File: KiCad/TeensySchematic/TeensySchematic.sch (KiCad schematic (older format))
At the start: 4 parts, among them J1 LEFT_ESC, J2 RIGHT_ESC, U1 Teensy3.2, U2 BNO055

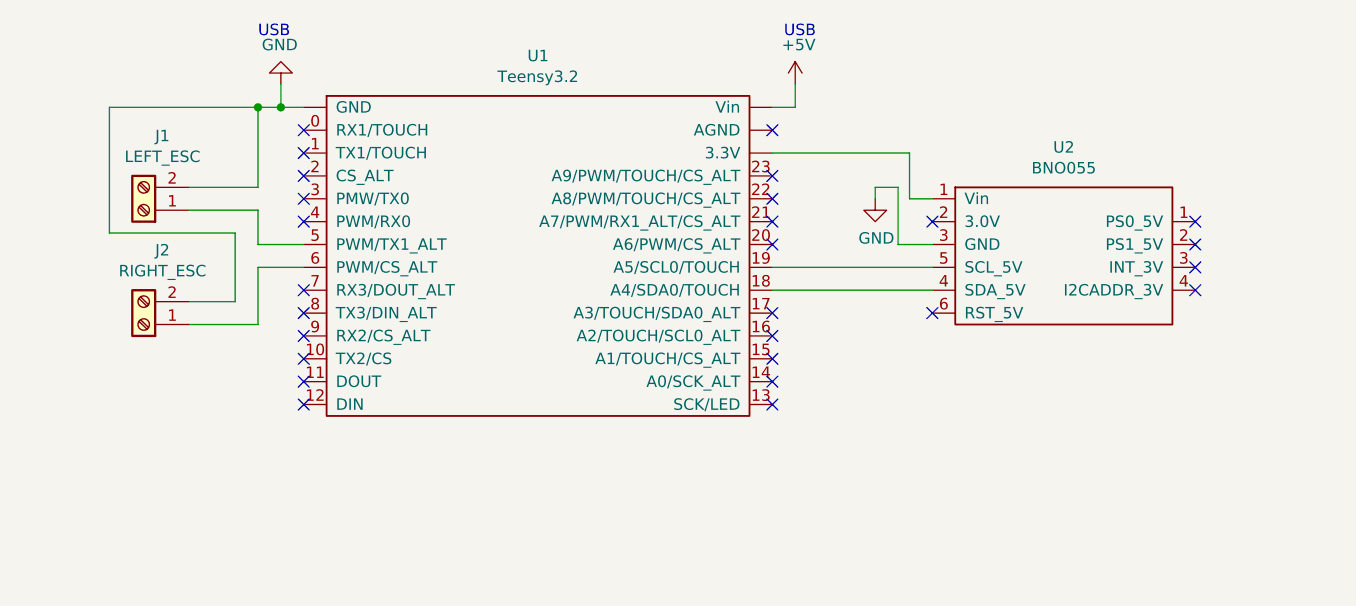
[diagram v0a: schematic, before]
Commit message: Added Ultimate GPS to the Teensy Schematic and updated our custom symbol library
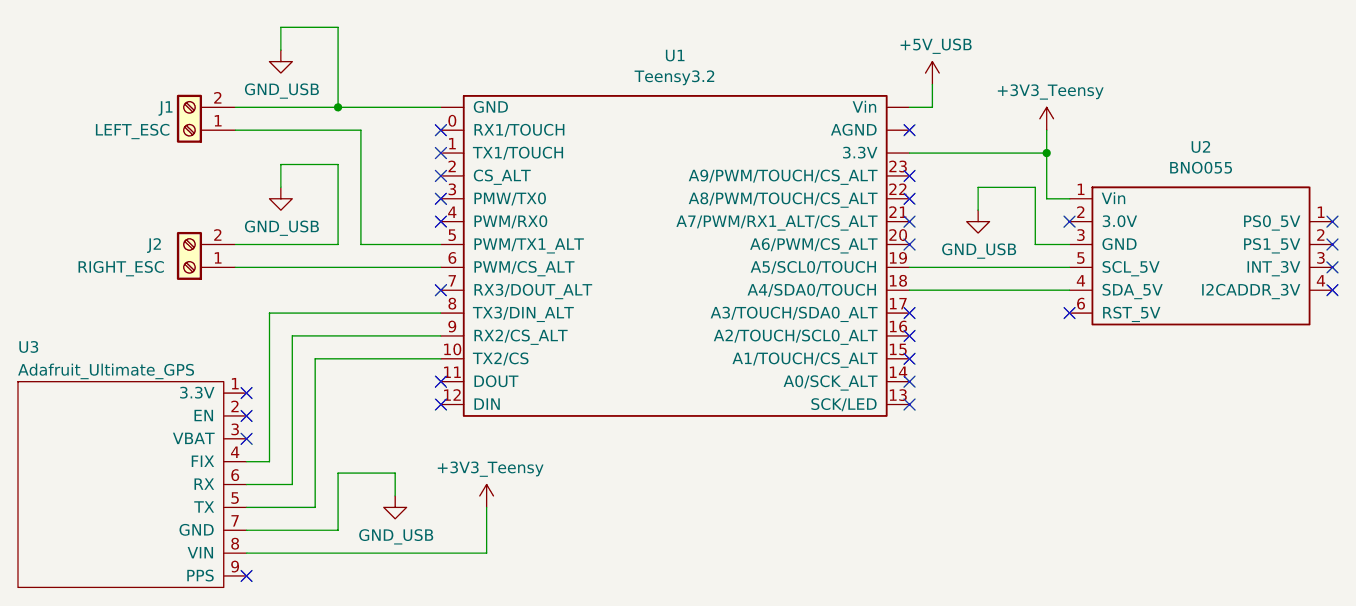
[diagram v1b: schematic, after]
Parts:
- added U3: Adafruit_Ultimate_GPS, symbol MCU_Module:Adafruit_Ultimate_GPS
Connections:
- net GND: now also U3.7 (GND)
- net +3V3: now reaches U2.1 (Vin)
- net +3V3: now also U1.~ (Vin), U3.8 (VIN)
- net at U2.4 (SDA_5V): now also U1.18 (A4/SDA0/TOUCH)
- net at U1.10 (TX2/CS): now also U3.5 (TX)
- net at U1.8 (TX3/DIN_ALT): now also U3.4 (FIX)
- net at U1.9 (RX2/CS_ALT): now also U3.6 (RX)
- no-connect marks 27 -> 28
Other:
- note removed: "USB"
- moved on the sheet: J1, J2, U1, U2
